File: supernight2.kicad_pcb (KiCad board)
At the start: 4 copper layers, 87.2 x 56.2 mm, 71 parts, among them J1 Conn_01x06_Female, J2 Conn_02x04_Odd_Even, Q1 BC847C, Q2 DMN3010LK3, Q3 DMN3010LK3, SW1 SW_SPST, U1 ESP32, U2 LMR33640ADDA, U3 LMR33610ADDA, U4 EL7202CN

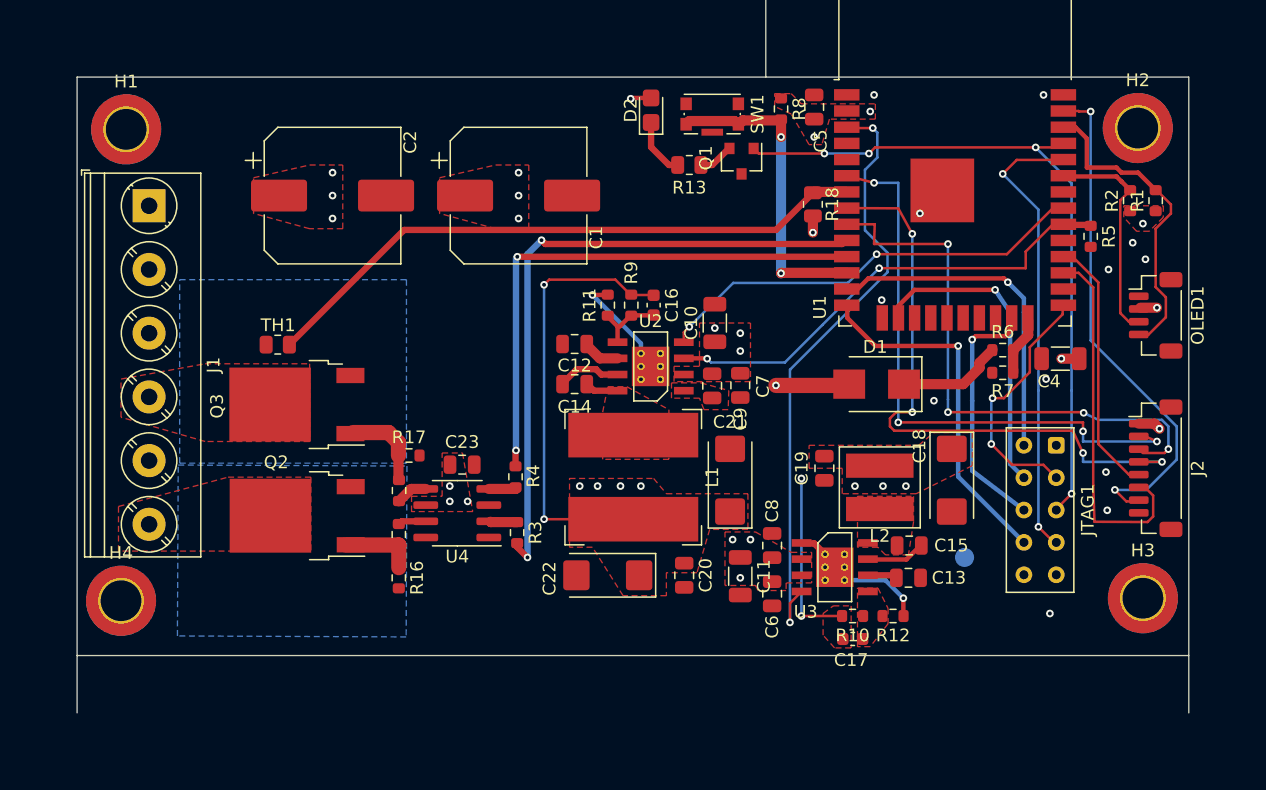
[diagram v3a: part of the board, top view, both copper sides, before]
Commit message: adding therm vias and silk markings
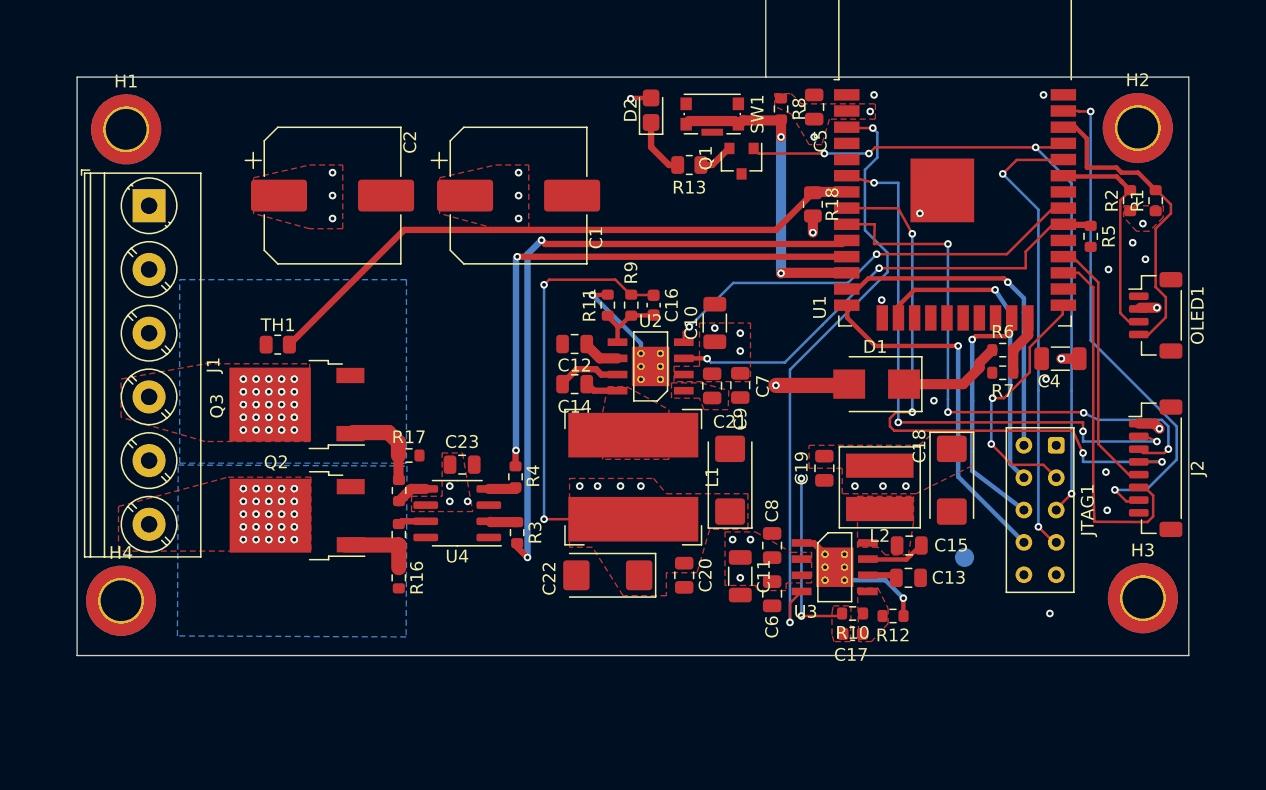
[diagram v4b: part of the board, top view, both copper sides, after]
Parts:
- moved C17 0.40 mm to (176.6, 113.3)
- moved R10 0.20 mm to (176.6, 111.7)
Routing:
- net /MOSFET_DRIVE/LED_L_2: vias 0 -> 25
- net /MOSFET_DRIVE/LED_L_1: vias 0 -> 25
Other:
- board size 87.2 x 56.2 mm -> 87.2 x 51.8 mm
- board text added: "GND"
- board text added: "LED +"
- board text added: "LED -"
- board text added: "VIN"
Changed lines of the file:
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@@
   (general
     (thickness 1.6)
-    (drawings 6)
-    (tracks 358)
+    (drawings 12)
+    (tracks 408)
     (zones 0)
     (modules 71)
@@
   )
   (module Resistor_SMD:R_0603_1608Metric (layer F.Cu)
-    (at 176.614 111.897)
+    (at 176.614 111.7)
     (descr "Resistor SMD 0603 (1608 Metric), square (rectangular) end terminal, IPC_7351 nominal, (Body size source: IPC-SM-782 page 72, https://www.pcb-3d.com/wordpress/wp-content/uploads/ipc-sm-782a_amendment_1_and_2.pdf), generated with kicad-footprint-generator")
     (tags resistor)
@@
   )
   (module Capacitor_SMD:C_0603_1608Metric (layer F.Cu)
-    (at 176.625 113.7)
+    (at 176.625 113.3)
     (descr "Capacitor SMD 0603 (1608 Metric), square (rectangular) end terminal, IPC_7351 nominal, (Body size source: IPC-SM-782 page 76, https://www.pcb-3d.com/wordpress/wp-content/uploads/ipc-sm-782a_amendment_1_and_2.pdf), generated with kicad-footprint-generator")
     (tags capacitor)
@@
     )
   )
+  (gr_text GND (at 126.6 84.9) (layer B.SilkS)
+    (effects (font (size 1.5 1.5) (thickness 0.3)) (justify mirror))
+  )
+  (gr_text VIN (at 126.4 79.9) (layer B.SilkS)
+    (effects (font (size 1.5 1.5) (thickness 0.3)) (justify mirror))
+  )
+  (gr_text "LED +" (at 127.4 99.7) (layer B.SilkS)
+    (effects (font (size 1.5 1.5) (thickness 0.3)) (justify mirror))
+  )
+  (gr_text "LED -" (at 127.4 104.7) (layer B.SilkS)
+    (effects (font (size 1.5 1.5) (thickness 0.3)) (justify mirror))
+  )
+  (gr_text "LED -" (at 127.4 94.7) (layer B.SilkS)
+    (effects (font (size 1.5 1.5) (thickness 0.3)) (justify mirror))
+  )
+  (gr_text "LED +" (at 127.4 89.7) (layer B.SilkS)
+    (effects (font (size 1.5 1.5) (thickness 0.3)) (justify mirror))
+  )
   (dimension 33.2 (width 0.15) (layer Dwgs.User)
     (gr_text "33.200 mm" (at 186.4 53.950001) (layer Dwgs.User)
@@
   (gr_line (start 115.75 69.6) (end 203 69.6) (layer Edge.Cuts) (width 0.1))
   (gr_line (start 169.8 63.25) (end 169.8 69.6) (layer Edge.Cuts) (width 0.1))
-  (gr_line (start 115.75 119.5) (end 115.75 69.6) (layer Edge.Cuts) (width 0.1))
+  (gr_line (start 115.75 115) (end 115.75 69.6) (layer Edge.Cuts) (width 0.1))
   (gr_line (start 203 115) (end 115.75 115) (layer Edge.Cuts) (width 0.1))
-  (gr_line (start 203 69.6) (end 203 119.5) (layer Edge.Cuts) (width 0.1))
+  (gr_line (start 203 69.6) (end 203 115) (layer Edge.Cuts) (width 0.1))
+  (via (at 128.8 93.3) (size 0.6) (drill 0.3) (layers F.Cu B.Cu) (net 52))
+  (via (at 128.8 101.9) (size 0.6) (drill 0.3) (layers F.Cu B.Cu) (net 53))
   (via (at 181.9 80.3) (size 0.6) (drill 0.3) (layers F.Cu B.Cu) (net 1))
   (via (at 199.6 83.9) (size 0.6) (drill 0.3) (layers F.Cu B.Cu) (net 1))
@@
   (segment (start 171 73) (end 168 73) (width 0.8) (layer F.Cu) (net 51))
   (segment (start 163.55 73.3) (end 163.800001 73.049999) (width 0.8) (layer F.Cu) (net 51))
+  (via (at 129.8 93.3) (size 0.6) (drill 0.3) (layers F.Cu B.Cu) (net 52))
+  (via (at 130.8 93.3) (size 0.6) (drill 0.3) (layers F.Cu B.Cu) (net 52))
+  (via (at 131.8 93.3) (size 0.6) (drill 0.3) (layers F.Cu B.Cu) (net 52))
+  (via (at 132.8 93.3) (size 0.6) (drill 0.3) (layers F.Cu B.Cu) (net 52))
+  (via (at 128.8 94.3) (size 0.6) (drill 0.3) (layers F.Cu B.Cu) (net 52))
+  (via (at 129.8 94.3) (size 0.6) (drill 0.3) (layers F.Cu B.Cu) (net 52))
+  (via (at 130.8 94.3) (size 0.6) (drill 0.3) (layers F.Cu B.Cu) (net 52))
+  (via (at 131.8 94.3) (size 0.6) (drill 0.3) (layers F.Cu B.Cu) (net 52))
+  (via (at 132.8 94.3) (size 0.6) (drill 0.3) (layers F.Cu B.Cu) (net 52))
+  (via (at 128.8 95.3) (size 0.6) (drill 0.3) (layers F.Cu B.Cu) (net 52))
+  (via (at 129.8 95.3) (size 0.6) (drill 0.3) (layers F.Cu B.Cu) (net 52))
+  (via (at 130.8 95.3) (size 0.6) (drill 0.3) (layers F.Cu B.Cu) (net 52))
+  (via (at 131.8 95.3) (size 0.6) (drill 0.3) (layers F.Cu B.Cu) (net 52))
+  (via (at 132.8 95.3) (size 0.6) (drill 0.3) (layers F.Cu B.Cu) (net 52))
+  (via (at 128.8 96.3) (size 0.6) (drill 0.3) (layers F.Cu B.Cu) (net 52))
+  (via (at 129.8 96.3) (size 0.6) (drill 0.3) (layers F.Cu B.Cu) (net 52))
+  (via (at 130.8 96.3) (size 0.6) (drill 0.3) (layers F.Cu B.Cu) (net 52))
+  (via (at 131.8 96.3) (size 0.6) (drill 0.3) (layers F.Cu B.Cu) (net 52))
+  (via (at 132.8 96.3) (size 0.6) (drill 0.3) (layers F.Cu B.Cu) (net 52))
+  (via (at 128.8 97.3) (size 0.6) (drill 0.3) (layers F.Cu B.Cu) (net 52))
+  (via (at 129.8 97.3) (size 0.6) (drill 0.3) (layers F.Cu B.Cu) (net 52))
+  (via (at 130.8 97.3) (size 0.6) (drill 0.3) (layers F.Cu B.Cu) (net 52))
+  (via (at 131.8 97.3) (size 0.6) (drill 0.3) (layers F.Cu B.Cu) (net 52))
+  (via (at 132.8 97.3) (size 0.6) (drill 0.3) (layers F.Cu B.Cu) (net 52))
+  (via (at 129.8 101.9) (size 0.6) (drill 0.3) (layers F.Cu B.Cu) (net 53))
+  (via (at 130.8 101.9) (size 0.6) (drill 0.3) (layers F.Cu B.Cu) (net 53))
+  (via (at 131.8 101.9) (size 0.6) (drill 0.3) (layers F.Cu B.Cu) (net 53))
+  (via (at 132.8 101.9) (size 0.6) (drill 0.3) (layers F.Cu B.Cu) (net 53))
+  (via (at 128.8 102.9) (size 0.6) (drill 0.3) (layers F.Cu B.Cu) (net 53))
+  (via (at 129.8 102.9) (size 0.6) (drill 0.3) (layers F.Cu B.Cu) (net 53))
+  (via (at 130.8 102.9) (size 0.6) (drill 0.3) (layers F.Cu B.Cu) (net 53))
+  (via (at 131.8 102.9) (size 0.6) (drill 0.3) (layers F.Cu B.Cu) (net 53))
+  (via (at 132.8 102.9) (size 0.6) (drill 0.3) (layers F.Cu B.Cu) (net 53))
+  (via (at 128.8 103.9) (size 0.6) (drill 0.3) (layers F.Cu B.Cu) (net 53))
+  (via (at 129.8 103.9) (size 0.6) (drill 0.3) (layers F.Cu B.Cu) (net 53))
+  (via (at 130.8 103.9) (size 0.6) (drill 0.3) (layers F.Cu B.Cu) (net 53))
+  (via (at 131.8 103.9) (size 0.6) (drill 0.3) (layers F.Cu B.Cu) (net 53))
+  (via (at 132.8 103.9) (size 0.6) (drill 0.3) (layers F.Cu B.Cu) (net 53))
+  (via (at 128.8 104.9) (size 0.6) (drill 0.3) (layers F.Cu B.Cu) (net 53))
+  (via (at 129.8 104.9) (size 0.6) (drill 0.3) (layers F.Cu B.Cu) (net 53))
+  (via (at 130.8 104.9) (size 0.6) (drill 0.3) (layers F.Cu B.Cu) (net 53))
+  (via (at 131.8 104.9) (size 0.6) (drill 0.3) (layers F.Cu B.Cu) (net 53))
+  (via (at 132.8 104.9) (size 0.6) (drill 0.3) (layers F.Cu B.Cu) (net 53))
+  (via (at 128.8 105.9) (size 0.6) (drill 0.3) (layers F.Cu B.Cu) (net 53))
+  (via (at 129.8 105.9) (size 0.6) (drill 0.3) (layers F.Cu B.Cu) (net 53))
+  (via (at 130.8 105.9) (size 0.6) (drill 0.3) (layers F.Cu B.Cu) (net 53))
+  (via (at 131.8 105.9) (size 0.6) (drill 0.3) (layers F.Cu B.Cu) (net 53))
+  (via (at 132.8 105.9) (size 0.6) (drill 0.3) (layers F.Cu B.Cu) (net 53))
   (segment (start 150.2875 104.5275) (end 148.2275 104.5275) (width 0.8) (layer F.Cu) (net 54))
   (segment (start 148.2275 104.5275) (end 148.2 104.5) (width 0.8) (layer F.Cu) (net 54))
@@
     (polygon
       (pts
-        (xy 179.4 111.3) (xy 179.4 112.5) (xy 178 114.3) (xy 177 114.3) (xy 177 109.7)
+        (xy 179.4 111.3) (xy 179.4 112.5) (xy 178.1 113.9) (xy 177.1 113.9) (xy 177 109.7)
         (xy 178.6 109.7)
       )
@@
     (polygon
       (pts
-        (xy 176.5 114.4) (xy 175.2 114.4) (xy 174.3 113.4) (xy 174.3 111.7) (xy 175.1 111.1)
+        (xy 176.45 113.9) (xy 175.15 113.9) (xy 175 113.35) (xy 175 111.65) (xy 175.1 111.1)
         (xy 176.5 111.1)
       )
